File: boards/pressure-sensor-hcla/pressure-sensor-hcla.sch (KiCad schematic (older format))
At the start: 3 parts, among them J1 CONN_01X04, U1 HCLA-XXXX-DIP-X

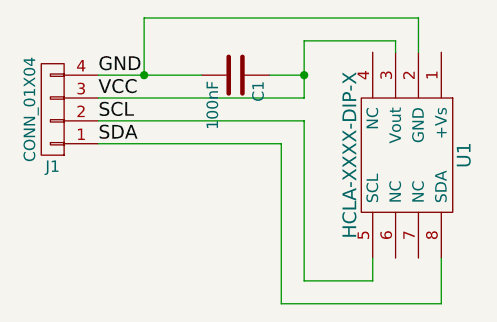
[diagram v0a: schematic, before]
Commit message: [pressure-sensor-hcla] Connect Vcc to +Vs Pin (not Vout)
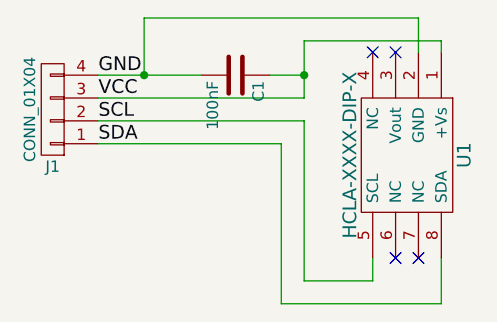
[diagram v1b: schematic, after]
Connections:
- net VCC: now also U1.1 (+Vs); no longer U1.3 (Vout)
- no-connect marks 0 -> 4
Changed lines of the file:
@@
 LIBS:valves
 LIBS:pressure-sensor-hcla
+LIBS:pressure-sensor-hcla-cache
 EELAYER 25 0
 EELAYER END
@@
 	2100 1150 2100 900
 Wire Wire Line
-	2100 900  2500 900
-Wire Wire Line
-	2500 900  2500 950
-Wire Wire Line
 	1950 1050 2100 1050
 Connection ~ 2100 1050
@@
 Text Label 1200 1350 0    60   ~ 0
 SDA
+NoConn ~ 2400 950
+NoConn ~ 2500 950
+NoConn ~ 2600 1850
+NoConn ~ 2500 1850
+Wire Wire Line
+	2100 900  2700 900
+Wire Wire Line
+	2700 900  2700 950
 $EndSCHEMATC
